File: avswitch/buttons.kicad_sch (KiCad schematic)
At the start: 16 parts, among them J701 CTRL_OUT, J702 CTRL_IN, J703 Conn_01x02, J704 Conn_01x04

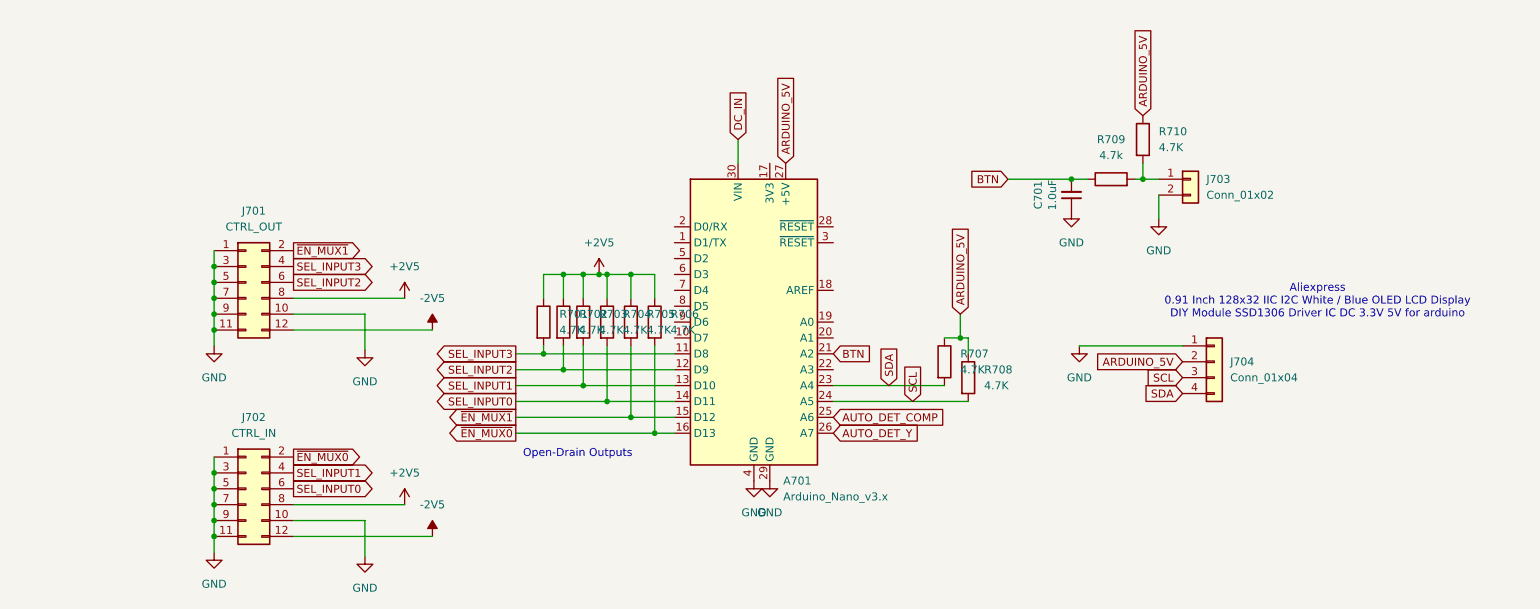
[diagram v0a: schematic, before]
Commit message: Recalculate for ceramic cap dc bias
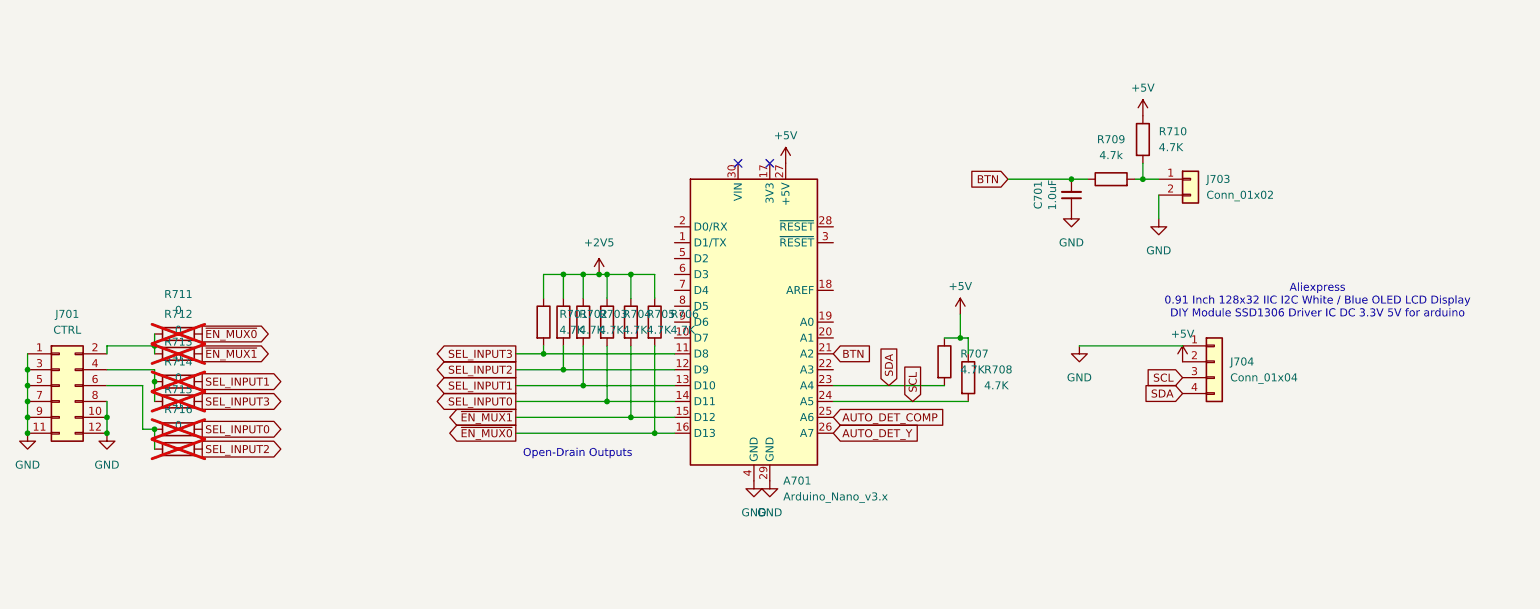
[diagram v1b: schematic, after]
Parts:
- removed J702: CTRL_IN, Connector_IDC:IDC-Header_2x06_P2.54mm_Horizontal, symbol Connector_Generic:Conn_02x06_Odd_Even
- added R711, R712, R713, R714, R715, R716: 0, Resistor_SMD:R_0805_2012Metric, symbol Device:R
- J701: value CTRL_OUT -> CTRL; footprint Connector_IDC:IDC-Header_2x06_P2.54mm_Horizontal -> avswitch:amphenol-HLW12R-2C7LF
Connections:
- net -2V5 is gone; now on net GND: J701.12 (Pin_12)
- net +2V5: no longer J701.8 (Pin_8)
- net GND: now also J701.8 (Pin_8)
- net SEL_INPUT0: now also R715.2
- net SEL_INPUT1: now also R713.2
- net SEL_INPUT2: now also R716.2; no longer J701.6 (Pin_6)
- net SEL_INPUT3: now also R714.2; no longer J701.4 (Pin_4)
- net ~{EN_MUX0}: now also R711.2
- net ~{EN_MUX1}: now also R712.2; no longer J701.2 (Pin_2)
- net ARDUINO_5V renamed +5V
- net DC_IN: no longer names the net of A701.30 (VIN)
- new net: J701.2 (Pin_2), R711.1, R712.1
- new net: J701.4 (Pin_4), R713.1, R714.1
- new net: J701.6 (Pin_6), R715.1, R716.1
- no-connect marks 0 -> 2

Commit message: PCB Layout nearing completion
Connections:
- net AUTO_DET_COMP: now also A701.20 (A1); no longer A701.25 (A6)
- net AUTO_DET_Y: now also A701.19 (A0); no longer A701.26 (A7)
- net BTN: now also A701.26 (A7); no longer A701.21 (A2)
- net SEL_INPUT0: now also A701.11 (D8), R702.2; no longer A701.14 (D11), R704.2
- net SEL_INPUT1: now also R704.2; no longer R703.2
- net SEL_INPUT2: now also A701.10 (D7), R701.2; no longer A701.12 (D9), R702.2
- net SEL_INPUT3: now also A701.12 (D9), R703.2; no longer A701.11 (D8), R701.2
- net ~{EN_MUX0}: now also A701.14 (D11), R705.2; no longer A701.16 (D13), R706.2
- net ~{EN_MUX1}: now also R706.2; no longer R705.2
- net CC1: now reaches A701.22 (A3)
- new net CC2: A701.21 (A2)
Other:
- note added: "EN_MUX0, SEL_INPUT0, SEL_INPUT1 is on current board EN_MUX1, SEL_INPUT2, SEL_INPUT3 is on other board"
- moved on the sheet: R701, R702, R703, R704, R705, R706

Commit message: V0.1 ordered from jlpcb
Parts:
- R701, R702, R703, R704, R705, R706, R707, R708, R710: value 4.7K -> 4.7k
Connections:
- net AUTO_DET_COMP: now also J701.12 (Pin_12)
- net AUTO_DET_Y: now also J701.10 (Pin_10)
- net GND: no longer J701.10 (Pin_10), J701.12 (Pin_12)
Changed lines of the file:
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@@
 	)
 	(junction
-		(at 41.275 97.79)
-		(diameter 0)
-		(color 0 0 0 0)
-	)
-	(junction
 		(at 117.475 87.63)
 		(diameter 0)
@@
 	)
 	(junction
-		(at 41.275 95.25)
-		(diameter 0)
-		(color 0 0 0 0)
-	)
-	(junction
 		(at 114.3 69.85)
 		(diameter 0)
@@
 	(wire
 		(pts
+			(xy 41.275 92.71) (xy 45.72 92.71)
+		)
+		(stroke
+			(width 0)
+			(type default)
+		)
+	)
+	(wire
+		(pts
 			(xy 41.275 87.63) (xy 48.895 87.63)
 		)
@@
 	(wire
 		(pts
-			(xy 41.275 92.71) (xy 41.275 95.25)
+			(xy 43.18 95.25) (xy 43.18 104.14)
 		)
 		(stroke
@@
 	(wire
 		(pts
-			(xy 48.895 87.63) (xy 48.895 89.535)
+			(xy 41.275 106.68) (xy 43.18 106.68)
 		)
 		(stroke
@@
 	(wire
 		(pts
-			(xy 106.68 90.17) (xy 121.285 90.17)
+			(xy 48.895 87.63) (xy 48.895 89.535)
 		)
 		(stroke
@@
 	(wire
 		(pts
-			(xy 41.275 95.25) (xy 41.275 97.79)
+			(xy 106.68 90.17) (xy 121.285 90.17)
 		)
 		(stroke
@@
 	(wire
 		(pts
+			(xy 41.275 95.25) (xy 43.18 95.25)
+		)
+		(stroke
+			(width 0)
+			(type default)
+		)
+	)
+	(wire
+		(pts
 			(xy 207.01 54.61) (xy 207.01 57.15)
 		)
@@
 	(wire
 		(pts
+			(xy 41.275 97.79) (xy 41.275 106.68)
+		)
+		(stroke
+			(width 0)
+			(type default)
+		)
+	)
+	(wire
+		(pts
 			(xy 28.575 92.71) (xy 28.575 95.25)
 		)
@@
 		)
 	)
+	(global_label "AUTO_DET_COMP"
+		(shape input)
+		(at 43.18 106.68 0)
+		(fields_autoplaced yes)
+		(effects
+			(font
+				(size 1.27 1.27)
+			)
+			(justify left)
+		)
+		(property "Intersheetrefs" "${INTERSHEET_REFS}"
+			(at 61.5261 106.68 0)
+			(effects
+				(font
+					(size 1.27 1.27)
+				)
+				(justify left)
+				(hide yes)
+			)
+		)
+	)
 	(global_label "SDA"
 		(shape input)
@@
 		)
 	)
+	(global_label "AUTO_DET_Y"
+		(shape input)
+		(at 43.18 104.14 0)
+		(fields_autoplaced yes)
+		(effects
+			(font
+				(size 1.27 1.27)
+			)
+			(justify left)
+		)
+		(property "Intersheetrefs" "${INTERSHEET_REFS}"
+			(at 57.2928 104.14 0)
+			(effects
+				(font
+					(size 1.27 1.27)
+				)
+				(justify left)
+				(hide yes)
+			)
+		)
+	)
 	(global_label "AUTO_DET_COMP"
 		(shape input)
@@
 			)
 		)
-		(property "Value" "4.7K"
+		(property "Value" "4.7k"
 			(at 116.84 78.7399 0)
 			(effects
@@
 			)
 		)
-		(property "Value" "4.7K"
+		(property "Value" "4.7k"
 			(at 120.015 78.7399 0)
 			(effects
@@
 			)
 		)
-		(property "Value" "4.7K"
+		(property "Value" "4.7k"
 			(at 181.61 90.1699 0)
 			(effects
@@
 	)
 	(symbol
-		(lib_id "power:GND")
-		(at 41.275 97.79 0)
-		(unit 1)
-		(exclude_from_sim no)
-		(in_bom yes)
-		(on_board yes)
-		(dnp no)
-		(fields_autoplaced yes)
-		(property "Reference" "#PWR0703"
-			(at 41.275 104.14 0)
-			(effects
-				(font
-					(size 1.27 1.27)
-				)
-				(hide yes)
-			)
-		)
-		(property "Value" "GND"
-			(at 41.275 102.87 0)
-			(effects
-				(font
-					(size 1.27 1.27)
-				)
-			)
-		)
-		(property "Footprint" ""
-			(at 41.275 97.79 0)
-			(effects
-				(font
-					(size 1.27 1.27)
-				)
-				(hide yes)
-			)
-		)
-		(property "Datasheet" ""
-			(at 41.275 97.79 0)
-			(effects
-				(font
-					(size 1.27 1.27)
-				)
-				(hide yes)
-			)
-		)
-		(property "Description" "Power symbol creates a global label with name \"GND\" , ground"
-			(at 41.275 97.79 0)
-			(effects
-				(font
-					(size 1.27 1.27)
-				)
-				(hide yes)
-			)
-		)
-		(pin "1"
-		)
-		(instances
-			(project "avswitch"
-				(path "/27d99f64-5b59-4054-806e-9fbbdd7153e5/cd0307b4-4503-4185-ab78-be813a4c5223"
-					(reference "#PWR0703")
-					(unit 1)
-				)
-			)
-		)
-	)
-	(symbol
 		(lib_id "Device:R")
 		(at 111.125 77.47 0)
@@
 			)
 		)
-		(property "Value" "4.7K"
+		(property "Value" "4.7k"
 			(at 113.665 78.7399 0)
 			(effects
@@
 			)
 		)
-		(property "Value" "4.7K"
+		(property "Value" "4.7k"
 			(at 209.55 52.0699 0)
 			(effects
@@
 			)
 		)
-		(property "Value" "4.7K"
+		(property "Value" "4.7k"
 			(at 127.635 78.7399 0)
 			(effects
@@
 			)
 		)
-		(property "Value" "4.7K"
+		(property "Value" "4.7k"
 			(at 123.825 78.7399 0)
 			(effects
@@
 			)
 		)
-		(property "Value" "4.7K"
+		(property "Value" "4.7k"
 			(at 131.445 78.7399 0)
 			(effects
@@
 	(symbol
 		(lib_id "power:GND")
+		(at 45.72 92.71 0)
+		(unit 1)
+		(exclude_from_sim no)
+		(in_bom yes)
+		(on_board yes)
+		(dnp no)
+		(fields_autoplaced yes)
+		(property "Reference" "#PWR0703"
+			(at 45.72 99.06 0)
+			(effects
+				(font
+					(size 1.27 1.27)
+				)
+				(hide yes)
+			)
+		)
+		(property "Value" "GND"
+			(at 45.72 97.79 0)
+			(effects
+				(font
+					(size 1.27 1.27)
+				)
+			)
+		)
+		(property "Footprint" ""
+			(at 45.72 92.71 0)
+			(effects
+				(font
+					(size 1.27 1.27)
+				)
+				(hide yes)
+			)
+		)
+		(property "Datasheet" ""
+			(at 45.72 92.71 0)
+			(effects
+				(font
+					(size 1.27 1.27)
+				)
+				(hide yes)
+			)
+		)
+		(property "Description" "Power symbol creates a global label with name \"GND\" , ground"
+			(at 45.72 92.71 0)
+			(effects
+				(font
+					(size 1.27 1.27)
+				)
+				(hide yes)
+			)
+		)
+		(pin "1"
+		)
+		(instances
+			(project "avswitch"
+				(path "/27d99f64-5b59-4054-806e-9fbbdd7153e5/cd0307b4-4503-4185-ab78-be813a4c5223"
+					(reference "#PWR0703")
+					(unit 1)
+				)
+			)
+		)
+	)
+	(symbol
+		(lib_id "power:GND")
 		(at 28.575 97.79 0)
 		(unit 1)
@@
 			)
 		)
-		(property "Value" "4.7K"
+		(property "Value" "4.7k"
 			(at 177.8 87.6299 0)
 			(effects
